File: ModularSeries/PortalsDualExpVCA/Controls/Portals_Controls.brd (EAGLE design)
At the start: 48.5 x 100 mm, 17 parts, among them SW1 SPDT_SWITCHDW1, SW2 SPDT_SWITCHDW1

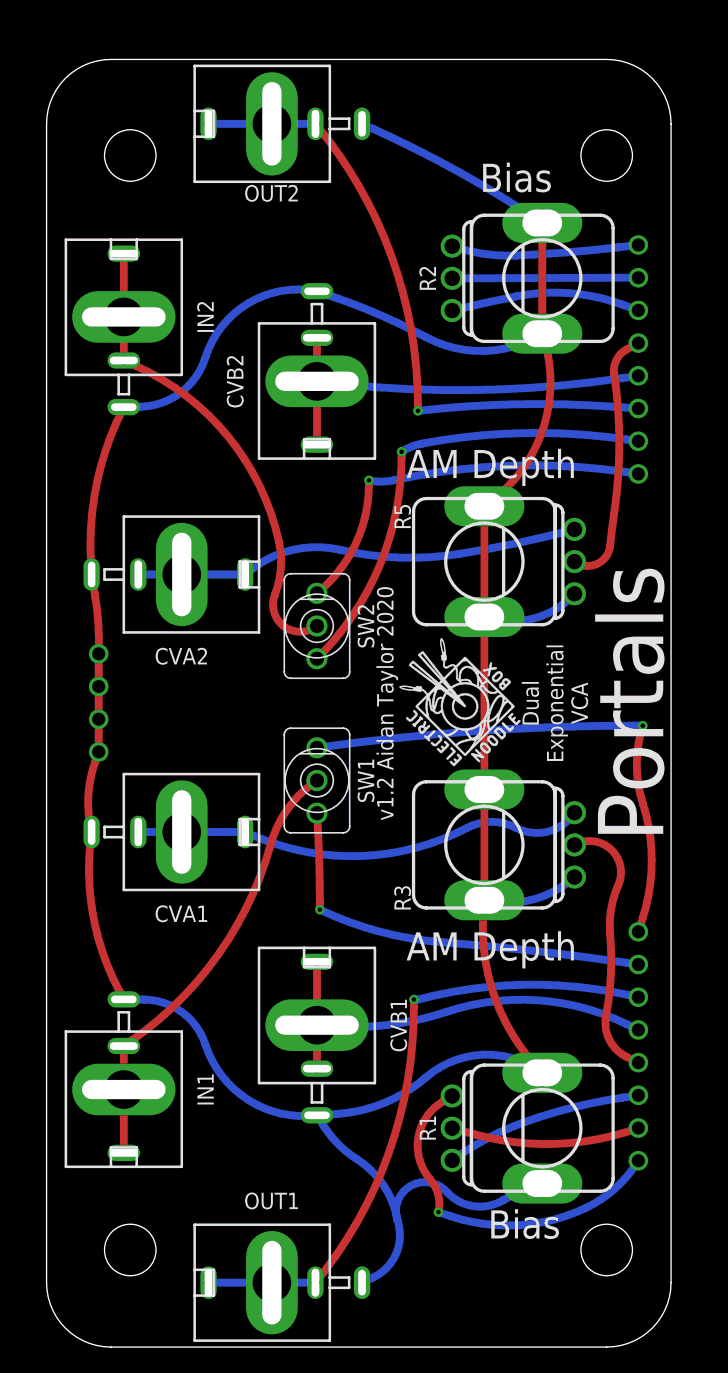
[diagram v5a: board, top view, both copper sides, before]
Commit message: Mirrors and Portals Renders brought up to date
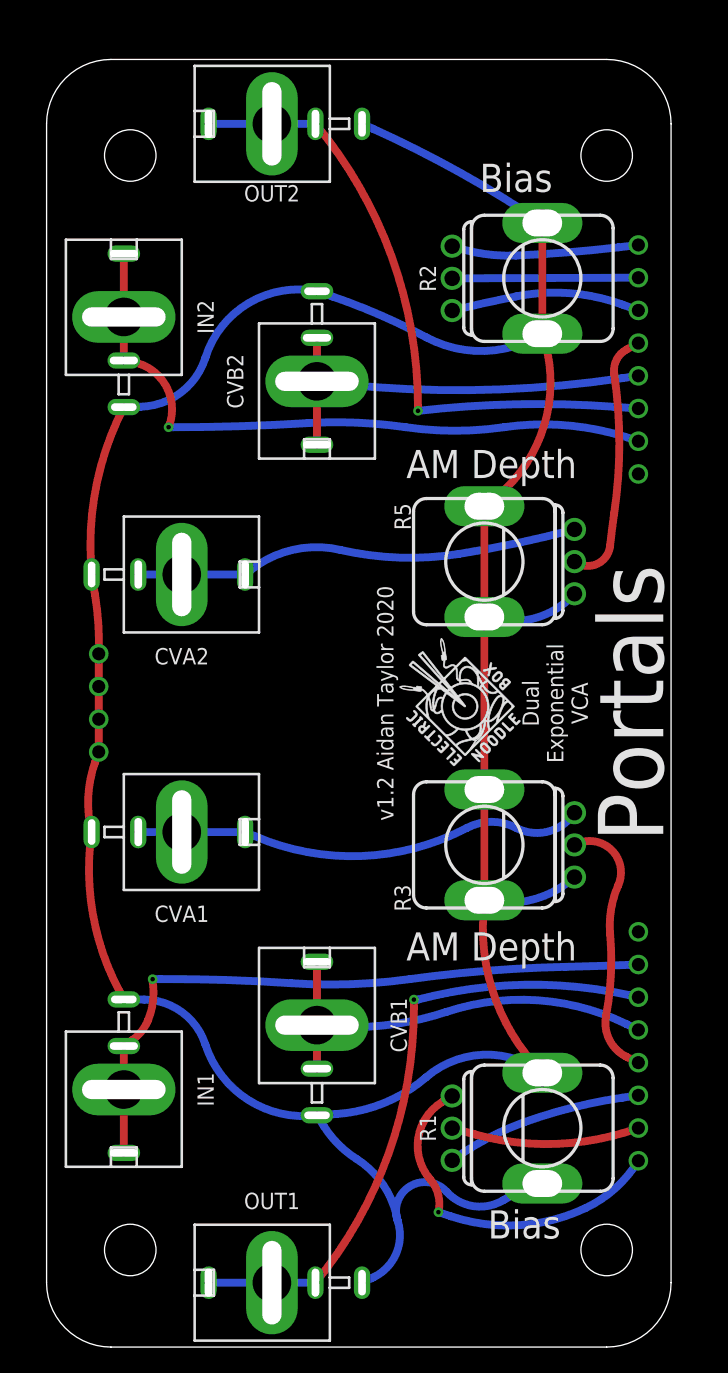
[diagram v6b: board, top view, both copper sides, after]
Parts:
- removed SW1, SW2: SPDT_SWITCHDW1, ElectricNoodleBox:MICRODPDT-DW1
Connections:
- removed net N$18: BOARD1.INVA, SW1.C3
- removed net N$20: BOARD1.SIB, SW2.C1
- removed net N$21: BOARD1.INVB, SW2.C3
- removed net N$22: IN2.CONN, IN2.T1, IN2.T2, SW2.C2
- net N$10: now also BOARD1.SIB, IN2.CONN, IN2.T1, IN2.T2; no longer BOARD1.SIA, SW1.C1
- net N$9: now also BOARD1.SIA; no longer SW1.C2
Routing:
- net N$18: track 41.4 -> 0.00 mm, vias 1 -> 0
- net N$20: track 35.9 -> 0.00 mm, vias 1 -> 0
- net N$22: track 35.1 -> 0.00 mm
- net N$21: track 30.6 -> 0.00 mm, vias 1 -> 0
- net N$10: track 32.7 -> 51.3 mm
- net N$9: track 33.8 -> 52.1 mm, vias 0 -> 1
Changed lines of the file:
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@@
 <setting verticaltext="up"/>
 </settings>
-<grid distance="12.5" unitdist="mil" unit="mm" style="lines" multiple="1" display="no" altdistance="5" altunitdist="mil" altunit="mil"/>
+<grid distance="12.5" unitdist="mil" unit="mil" style="lines" multiple="1" display="no" altdistance="5" altunitdist="mil" altunit="mil"/>
 <layers>
 <layer number="1" name="Top" color="4" fill="1" visible="yes" active="yes"/>
@@
 <layer number="17" name="Pads" color="2" fill="1" visible="yes" active="yes"/>
 <layer number="18" name="Vias" color="2" fill="1" visible="yes" active="yes"/>
-<layer number="19" name="Unrouted" color="6" fill="1" visible="no" active="yes"/>
+<layer number="19" name="Unrouted" color="6" fill="1" visible="yes" active="yes"/>
 <layer number="20" name="Dimension" color="24" fill="1" visible="yes" active="yes"/>
 <layer number="21" name="tPlace" color="7" fill="1" visible="yes" active="yes"/>
@@
 <attribute name="VALUE" x="42.62" y="68.62" size="1.27" layer="27" rot="R90" align="center"/>
 </element>
-<element name="SW1" library="ElectricNoodleBox" package="MICRODPDT-DW1" value="SPDT_SWITCHDW1" x="22" y="44" smashed="yes">
-<attribute name="NAME" x="25.81" y="44" size="1.27" layer="25" rot="R90" align="center"/>
-</element>
-<element name="SW2" library="ElectricNoodleBox" package="MICRODPDT-DW1" value="SPDT_SWITCHDW1" x="22" y="56" smashed="yes">
-<attribute name="NAME" x="25.81" y="56" size="1.27" layer="25" rot="R90" align="center"/>
-</element>
 <element name="CVA1" library="ElectricNoodleBox" package="NEWCOMBOJACK_PANEL" value="COMBI-JACKCINCHNANA" x="11.5" y="40" smashed="yes" rot="R270">
 <attribute name="NAME" x="11.5" y="33.65" size="1.27" layer="25" font="vector" align="center"/>
@@
 <wire x1="37.465" y1="81.5975" x2="32.5" y2="80.5" width="0.6096" layer="16" curve="2.428036"/>
 </signal>
-<signal name="N$9">
-<contactref element="SW1" pad="C2"/>
-<contactref element="IN1" pad="T2"/>
-<contactref element="IN1" pad="CONN"/>
-<contactref element="IN1" pad="T1"/>
-<wire x1="7" y1="23.38" x2="7" y2="20" width="0.6096" layer="1"/>
-<wire x1="7" y1="20" x2="7" y2="15.08" width="0.6096" layer="1"/>
-<wire x1="7" y1="23.38" x2="7.62" y2="23.8125" width="0.6096" layer="1"/>
-<wire x1="7.62" y1="23.8125" x2="18.415" y2="39.0525" width="0.6096" layer="1" curve="39.579809"/>
-<wire x1="18.415" y1="39.0525" x2="22" y2="44" width="0.6096" layer="1" curve="-40.812162"/>
-</signal>
-<signal name="N$10">
-<contactref element="BOARD1" pad="SIA"/>
-<contactref element="SW1" pad="C1"/>
-<wire x1="46.96" y1="29.71" x2="46.0375" y2="29.845" width="0.6096" layer="16"/>
-<wire x1="46.0375" y1="29.845" x2="31.75" y2="31.4325" width="0.6096" layer="16" curve="3.970917"/>
-<wire x1="31.75" y1="31.4325" x2="22.225" y2="33.9725" width="0.6096" layer="16" curve="-21.1534"/>
-<via x="22.225" y="33.9725" extent="1-16" drill="0.35"/>
-<wire x1="22.225" y1="33.9725" x2="22.225" y2="34.6075" width="0.6096" layer="1"/>
-<wire x1="22.225" y1="34.6075" x2="22" y2="41.46" width="0.6096" layer="1" curve="3.761232"/>
-</signal>
-<signal name="N$18">
-<contactref element="BOARD1" pad="INVA"/>
-<contactref element="SW1" pad="C3"/>
-<wire x1="46.96" y1="32.25" x2="47.3075" y2="33.3375" width="0.6096" layer="1"/>
-<wire x1="47.3075" y1="33.3375" x2="47.3075" y2="42.2275" width="0.6096" layer="1" curve="35.441543"/>
-<wire x1="47.3075" y1="42.2275" x2="47.3075" y2="48.26" width="0.6096" layer="1" curve="-35.4415"/>
-<via x="47.3075" y="48.26" extent="1-16" drill="0.35"/>
-<wire x1="47.3075" y1="48.26" x2="46.6725" y2="48.26" width="0.6096" layer="16"/>
-<wire x1="46.6725" y1="48.26" x2="22" y2="46.54" width="0.6096" layer="16" curve="7.975646"/>
-</signal>
 <signal name="N$19">
 <contactref element="BOARD1" pad="SOB"/>
@@
 <wire x1="18.5" y1="95" x2="21.88" y2="95" width="0.6096" layer="16"/>
 </signal>
-<signal name="N$20">
-<contactref element="BOARD1" pad="SIB"/>
-<contactref element="SW2" pad="C1"/>
-<wire x1="46.96" y1="70.35" x2="46.0375" y2="70.485" width="0.6096" layer="16"/>
-<wire x1="46.0375" y1="70.485" x2="30.1625" y2="70.1675" width="0.6096" layer="16" curve="18.942826"/>
-<wire x1="30.1625" y1="70.1675" x2="28.575" y2="69.5325" width="0.6096" layer="16" curve="22.368464"/>
-<via x="28.575" y="69.5325" extent="1-16" drill="0.35"/>
-<wire x1="28.575" y1="69.5325" x2="28.575" y2="69.215" width="0.6096" layer="1"/>
-<wire x1="28.575" y1="69.215" x2="22" y2="53.46" width="0.6096" layer="1" curve="-45.304272"/>
-</signal>
-<signal name="N$21">
-<contactref element="BOARD1" pad="INVB"/>
-<contactref element="SW2" pad="C3"/>
-<wire x1="46.96" y1="67.81" x2="46.0375" y2="67.945" width="0.6096" layer="16"/>
-<wire x1="46.0375" y1="67.945" x2="27.94" y2="67.31" width="0.6096" layer="16" curve="20.670409"/>
-<wire x1="27.94" y1="67.31" x2="26.035" y2="67.31" width="0.6096" layer="16" curve="-24.68957"/>
-<via x="26.035" y="67.31" extent="1-16" drill="0.35"/>
-<wire x1="26.035" y1="67.31" x2="26.035" y2="66.9925" width="0.6096" layer="1"/>
-<wire x1="26.035" y1="66.9925" x2="22" y2="58.54" width="0.6096" layer="1" curve="-51.037157"/>
-</signal>
-<signal name="N$22">
-<contactref element="SW2" pad="C2"/>
-<contactref element="IN2" pad="T2"/>
-<contactref element="IN2" pad="CONN"/>
-<contactref element="IN2" pad="T1"/>
-<wire x1="7" y1="84.92" x2="7" y2="80" width="0.6096" layer="1"/>
-<wire x1="7" y1="80" x2="7" y2="76.62" width="0.6096" layer="1"/>
-<wire x1="7" y1="76.62" x2="7.9375" y2="76.2" width="0.6096" layer="1"/>
-<wire x1="7.9375" y1="76.2" x2="19.05" y2="62.5475" width="0.6096" layer="1" curve="-53.447263"/>
-<wire x1="19.05" y1="62.5475" x2="18.7325" y2="58.42" width="0.6096" layer="1" curve="-33.638083"/>
-<wire x1="18.7325" y1="58.42" x2="22" y2="56" width="0.6096" layer="1" curve="149.386149"/>
-</signal>
 <signal name="N$1">
 <contactref element="BOARD1" pad="CVA2"/>
@@
 <wire x1="22" y1="75" x2="22" y2="70.08" width="0.6096" layer="1"/>
 </signal>
+<signal name="N$9">
+<contactref element="BOARD1" pad="SIA"/>
+<contactref element="IN1" pad="CONN"/>
+<contactref element="IN1" pad="T1"/>
+<contactref element="IN1" pad="T2"/>
+<wire x1="7" y1="15.08" x2="7" y2="20" width="0.6096" layer="1"/>
+<wire x1="7" y1="20" x2="7" y2="23.38" width="0.6096" layer="1"/>
+<wire x1="7" y1="23.38" x2="7.62" y2="23.8125" width="0.6096" layer="1"/>
+<wire x1="7.62" y1="23.8125" x2="8.89" y2="25.4" width="0.6096" layer="1" curve="32.882627"/>
+<wire x1="8.89" y1="25.4" x2="9.2075" y2="28.575" width="0.6096" layer="1" curve="33.015824"/>
+<wire x1="9.2075" y1="28.575" x2="9.238934375" y2="28.57185625" width="0.6096" layer="1" curve="-213.025812"/>
+<via x="9.238934375" y="28.57185625" extent="1-16" drill="0.35"/>
+<wire x1="9.238934375" y1="28.57185625" x2="9.8425" y2="28.575" width="0.6096" layer="16"/>
+<wire x1="9.8425" y1="28.575" x2="20.0025" y2="28.2575" width="0.6096" layer="16" curve="-4.176681"/>
+<wire x1="20.0025" y1="28.2575" x2="29.21" y2="28.575" width="0.6096" layer="16" curve="11.706419"/>
+<wire x1="29.21" y1="28.575" x2="41.275" y2="29.5275" width="0.6096" layer="16" curve="-6.628287"/>
+<wire x1="41.275" y1="29.5275" x2="46.96" y2="29.71" width="0.6096" layer="16" curve="1.277636"/>
+</signal>
+<signal name="N$10">
+<contactref element="BOARD1" pad="SIB"/>
+<contactref element="IN2" pad="CONN"/>
+<contactref element="IN2" pad="T1"/>
+<contactref element="IN2" pad="T2"/>
+<wire x1="7" y1="84.92" x2="7" y2="80" width="0.6096" layer="1"/>
+<wire x1="7" y1="80" x2="7" y2="76.62" width="0.6096" layer="1"/>
+<wire x1="7" y1="76.62" x2="7.62" y2="76.5175" width="0.6096" layer="1"/>
+<wire x1="7.62" y1="76.5175" x2="10.4775" y2="71.4375" width="0.6096" layer="1" curve="-102.509762"/>
+<via x="10.4775" y="71.4375" extent="1-16" drill="0.35"/>
+<wire x1="10.4775" y1="71.4375" x2="10.795" y2="71.4375" width="0.6096" layer="16"/>
+<wire x1="10.795" y1="71.4375" x2="21.2725" y2="71.755" width="0.6096" layer="16" curve="3.471409"/>
+<wire x1="21.2725" y1="71.755" x2="28.8925" y2="71.4375" width="0.6096" layer="16" curve="-11.714655"/>
+<wire x1="28.8925" y1="71.4375" x2="36.5125" y2="71.4375" width="0.6096" layer="16" curve="16.486501"/>
+<wire x1="36.5125" y1="71.4375" x2="46.96" y2="70.35" width="0.6096" layer="16" curve="-28.371749"/>
+</signal>
 </signals>

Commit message: Fields added and various updates to designs
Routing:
- added copper zone on layer 1, net AGND
- added copper zone on layer 16, net AGND
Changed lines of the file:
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@@
 <setting verticaltext="up"/>
 </settings>
-<grid distance="12.5" unitdist="mil" unit="mil" style="lines" multiple="1" display="no" altdistance="5" altunitdist="mil" altunit="mil"/>
+<grid distance="1" unitdist="mm" unit="mm" style="lines" multiple="1" display="no" altdistance="5" altunitdist="mil" altunit="mil"/>
 <layers>
 <layer number="1" name="Top" color="4" fill="1" visible="yes" active="yes"/>
@@
 <wire x1="8.5725" y1="26.9875" x2="13.335" y2="23.495" width="0.6096" layer="16" curve="-71.596806"/>
 <wire x1="13.335" y1="23.495" x2="22" y2="18" width="0.6096" layer="16" curve="79.341951"/>
+<polygon width="0.5" layer="1">
+<vertex x="1" y="0"/>
+<vertex x="50" y="0"/>
+<vertex x="50" y="100"/>
+<vertex x="1" y="100"/>
+</polygon>
+<polygon width="0.5" layer="16">
+<vertex x="1" y="0"/>
+<vertex x="50" y="0"/>
+<vertex x="50" y="100"/>
+<vertex x="1" y="100"/>
+</polygon>
 </signal>
 <signal name="N$4">
